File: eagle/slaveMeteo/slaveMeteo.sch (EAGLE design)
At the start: 33 parts, among them J1 RJ12RIGHTANGLE-I2C, Q1 CMA-4544PF-W, U2 MAX4466EXK+T, X1 1503_09

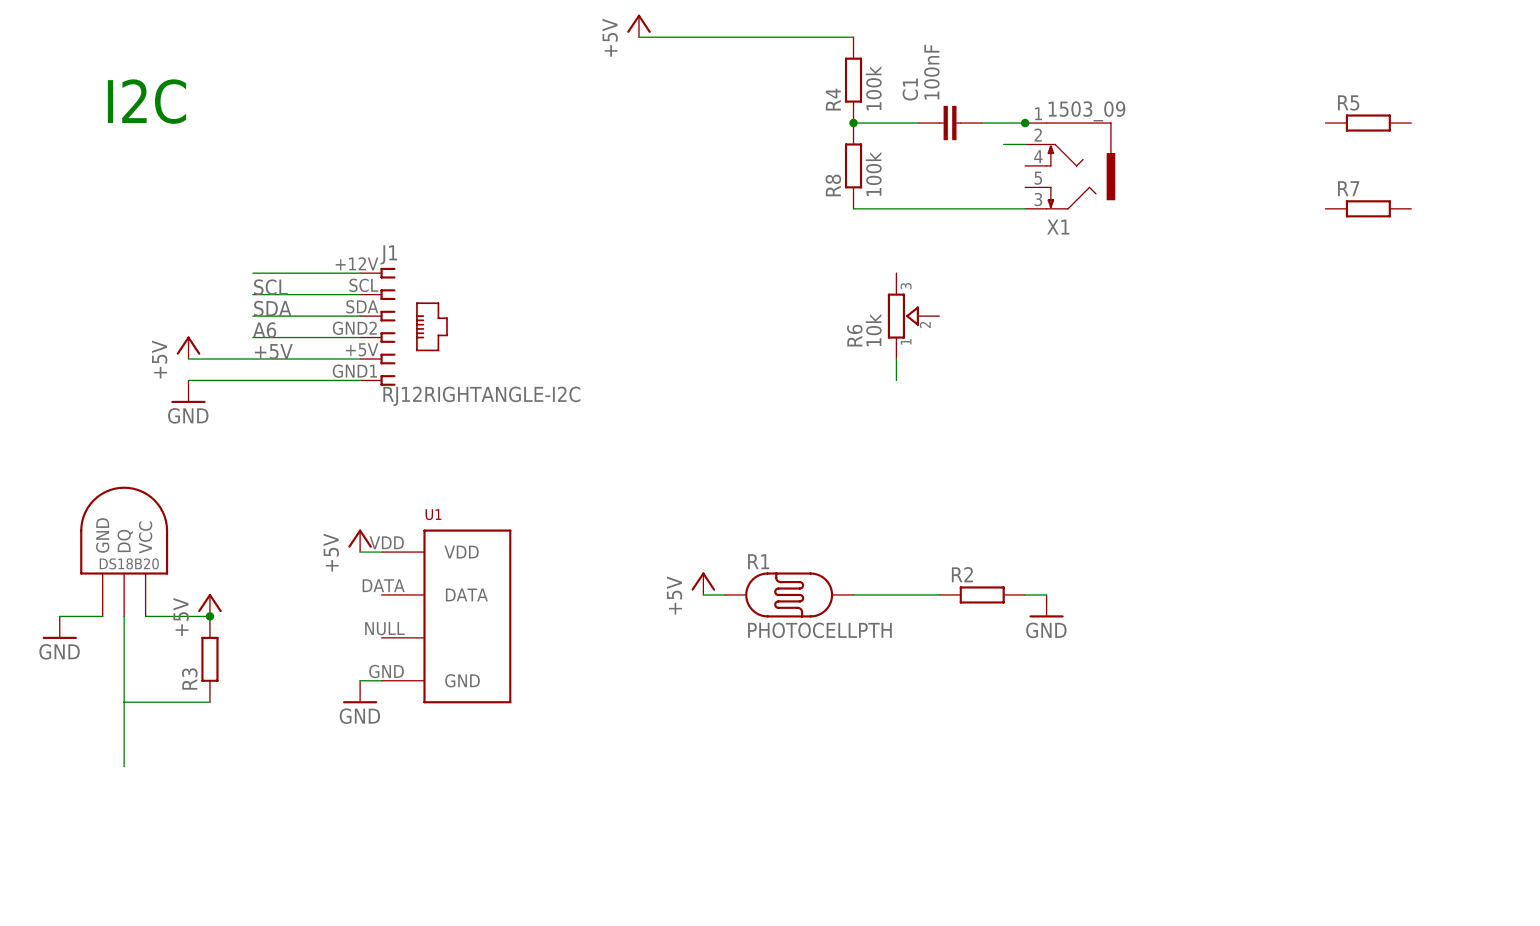
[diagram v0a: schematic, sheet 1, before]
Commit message: updated eagle libraries and readme, started designing meteo station
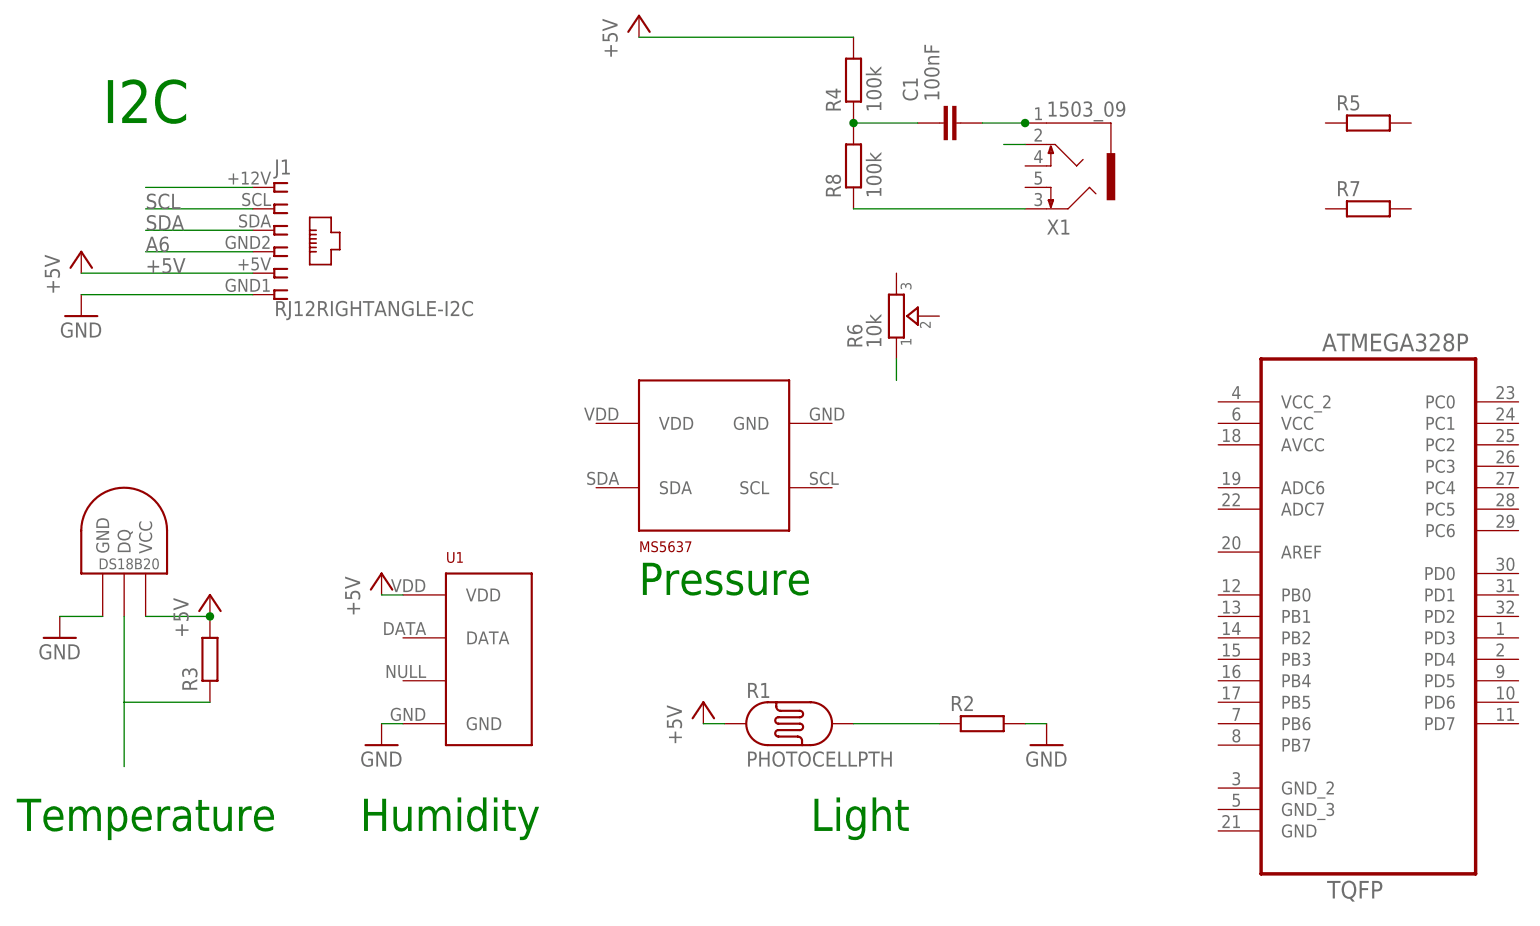
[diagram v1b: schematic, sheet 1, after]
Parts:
- added U$19: MS5637, MS5637:MS5637
- added U3: ATMEGA328P-AU, Ava:ATMEGA328P-AU
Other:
- note added: "Humidity"
- note added: "Light"
- note added: "Pressure"
- note added: "Temperature"
- moved on the sheet: J1, R1, R2, U1
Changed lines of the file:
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@@
 <?xml version="1.0" encoding="utf-8"?>
 <!DOCTYPE eagle SYSTEM "eagle.dtd">
-<eagle version="8.2.2">
+<eagle version="9.0.0">
 <drawing>
 <settings>
 <setting alwaysvectorfont="no"/>
+<setting keepoldvectorfont="yes"/>
 <setting verticaltext="up"/>
 </settings>
@@
 <part name="U$16" library="microbuilder" deviceset="GND" device=""/>
 <part name="P+7" library="microbuilder" deviceset="VCC" device=""/>
+<part name="U3" library="Ava" deviceset="ATMEGA328P-AU" device=""/>
+<part name="U$19" library="MS5637" deviceset="MS5637" device=""/>
 </parts>
 <sheets>
@@
 <plain>
 <text x="48.26" y="73.66" size="5.08" layer="91">I2C</text>
+<text x="38.1" y="-10.16" size="3.81" layer="91">Temperature</text>
+<text x="78.74" y="-10.16" size="3.81" layer="91">Humidity</text>
+<text x="132.08" y="-10.16" size="3.81" layer="91">Light</text>
+<text x="111.76" y="17.78" size="3.81" layer="91">Pressure</text>
 </plain>
 <instances>
-<instance part="GND8" gate="1" x="58.42" y="40.64"/>
-<instance part="J1" gate="G$1" x="81.28" y="50.8"/>
+<instance part="GND8" gate="1" x="45.72" y="50.8"/>
+<instance part="J1" gate="G$1" x="68.58" y="60.96"/>
 <instance part="U$1" gate="G$1" x="50.8" y="20.32"/>
-<instance part="U1" gate="G$1" x="91.44" y="15.24"/>
-<instance part="R1" gate="G$1" x="129.54" y="17.78"/>
-<instance part="R2" gate="G$1" x="152.4" y="17.78"/>
+<instance part="U1" gate="G$1" x="93.98" y="10.16"/>
+<instance part="R1" gate="G$1" x="129.54" y="2.54"/>
+<instance part="R2" gate="G$1" x="152.4" y="2.54"/>
 <instance part="R3" gate="G$1" x="60.96" y="10.16" rot="R90"/>
 <instance part="GND1" gate="1" x="43.18" y="12.7"/>
-<instance part="P+1" gate="1" x="58.42" y="48.26"/>
+<instance part="P+1" gate="1" x="45.72" y="58.42"/>
 <instance part="P+2" gate="1" x="60.96" y="17.78"/>
-<instance part="GND2" gate="1" x="78.74" y="5.08"/>
-<instance part="P+3" gate="1" x="78.74" y="25.4"/>
-<instance part="P+4" gate="1" x="119.38" y="20.32"/>
-<instance part="GND3" gate="1" x="160.02" y="15.24"/>
+<instance part="GND2" gate="1" x="81.28" y="0"/>
+<instance part="P+3" gate="1" x="81.28" y="20.32"/>
+<instance part="P+4" gate="1" x="119.38" y="5.08"/>
+<instance part="GND3" gate="1" x="160.02" y="0"/>
 <instance part="R6" gate="R" x="142.24" y="50.8" rot="R90"/>
 <instance part="X1" gate="G$1" x="162.56" y="68.58" rot="MR180"/>
@@
 <instance part="R8" gate="G$1" x="137.16" y="68.58" rot="R90"/>
 <instance part="P+5" gate="1" x="111.76" y="86.36"/>
+<instance part="U3" gate="A" x="198.12" y="17.78"/>
+<instance part="U$19" gate="G$1" x="121.92" y="35.56"/>
 </instances>
 <busses>
@@
 <segment>
 <pinref part="GND8" gate="1" pin="GND"/>
-<wire x1="78.74" y1="43.18" x2="58.42" y2="43.18" width="0.1524" layer="91"/>
+<wire x1="66.04" y1="53.34" x2="45.72" y2="53.34" width="0.1524" layer="91"/>
 <pinref part="J1" gate="G$1" pin="6"/>
 </segment>
@@
 <pinref part="U1" gate="G$1" pin="GND"/>
 <pinref part="GND2" gate="1" pin="GND"/>
-<wire x1="78.74" y1="7.62" x2="81.28" y2="7.62" width="0.1524" layer="91"/>
+<wire x1="81.28" y1="2.54" x2="83.82" y2="2.54" width="0.1524" layer="91"/>
 </segment>
 <segment>
 <pinref part="R2" gate="G$1" pin="2"/>
 <pinref part="GND3" gate="1" pin="GND"/>
-<wire x1="160.02" y1="17.78" x2="157.48" y2="17.78" width="0.1524" layer="91"/>
+<wire x1="160.02" y1="2.54" x2="157.48" y2="2.54" width="0.1524" layer="91"/>
 </segment>
 <segment>
@@
 <net name="SDA" class="0">
 <segment>
-<wire x1="78.74" y1="50.8" x2="66.04" y2="50.8" width="0.1524" layer="91"/>
-<label x="66.04" y="50.8" size="1.778" layer="95"/>
+<wire x1="66.04" y1="60.96" x2="53.34" y2="60.96" width="0.1524" layer="91"/>
+<label x="53.34" y="60.96" size="1.778" layer="95"/>
 <pinref part="J1" gate="G$1" pin="3"/>
 </segment>
@@
 <net name="SCL" class="0">
 <segment>
-<wire x1="78.74" y1="53.34" x2="66.04" y2="53.34" width="0.1524" layer="91"/>
-<label x="66.04" y="53.34" size="1.778" layer="95"/>
+<wire x1="66.04" y1="63.5" x2="53.34" y2="63.5" width="0.1524" layer="91"/>
+<label x="53.34" y="63.5" size="1.778" layer="95"/>
 <pinref part="J1" gate="G$1" pin="2"/>
 </segment>
@@
 <net name="A6" class="0">
 <segment>
-<wire x1="66.04" y1="48.26" x2="78.74" y2="48.26" width="0.1524" layer="91"/>
+<wire x1="53.34" y1="58.42" x2="66.04" y2="58.42" width="0.1524" layer="91"/>
 <pinref part="J1" gate="G$1" pin="4"/>
-<label x="66.04" y="48.26" size="1.778" layer="95"/>
+<label x="53.34" y="58.42" size="1.778" layer="95"/>
 </segment>
 </net>
@@
 <pinref part="R1" gate="G$1" pin="P$2"/>
 <pinref part="R2" gate="G$1" pin="1"/>
-<wire x1="137.16" y1="17.78" x2="147.32" y2="17.78" width="0.1524" layer="91"/>
+<wire x1="137.16" y1="2.54" x2="147.32" y2="2.54" width="0.1524" layer="91"/>
 </segment>
 </net>
@@
 <segment>
 <pinref part="J1" gate="G$1" pin="5"/>
-<wire x1="78.74" y1="45.72" x2="58.42" y2="45.72" width="0.1524" layer="91"/>
-<label x="66.04" y="45.72" size="1.778" layer="95"/>
+<wire x1="66.04" y1="55.88" x2="45.72" y2="55.88" width="0.1524" layer="91"/>
+<label x="53.34" y="55.88" size="1.778" layer="95"/>
 <pinref part="P+1" gate="1" pin="+5V"/>
 </segment>
@@
 <pinref part="U1" gate="G$1" pin="VDD"/>
 <pinref part="P+3" gate="1" pin="+5V"/>
-<wire x1="78.74" y1="22.86" x2="81.28" y2="22.86" width="0.1524" layer="91"/>
+<wire x1="81.28" y1="17.78" x2="83.82" y2="17.78" width="0.1524" layer="91"/>
 </segment>
 <segment>
 <pinref part="R1" gate="G$1" pin="P$1"/>
 <pinref part="P+4" gate="1" pin="+5V"/>
-<wire x1="119.38" y1="17.78" x2="121.92" y2="17.78" width="0.1524" layer="91"/>
+<wire x1="119.38" y1="2.54" x2="121.92" y2="2.54" width="0.1524" layer="91"/>
 </segment>
 <segment>
@@
 <segment>
 <pinref part="J1" gate="G$1" pin="1"/>
-<wire x1="78.74" y1="55.88" x2="66.04" y2="55.88" width="0.1524" layer="91"/>
+<wire x1="66.04" y1="66.04" x2="53.34" y2="66.04" width="0.1524" layer="91"/>
 </segment>
 </net>
@@
 <compatibility>
 <note version="8.2" severity="warning">
-Since Version 8.2, Eagle supports online libraries. The ids
+Since Version 8.2, EAGLE supports online libraries. The ids
 of those online libraries will not be understood (or retained)
 with this version.

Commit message: connected components on Slave meteo. Kept backup in case we still need a sound detector
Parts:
- removed C5: 10uF, microbuilder:CAP_CERAMIC0805
- removed FB1, FB2: FERRITE, microbuilder:FERRITE0805
- removed FID1, FID2: FIDUCIAL"", microbuilder:FIDUCIAL""
- removed JP1: (no value), microbuilder:HEADER-1X376MIL
- removed Q1: CMA-4544PF-W, microbuilder:ELECTRET
- removed R10, R11: 1K, microbuilder:RESISTOR0805
- removed R12, R13: 1M, microbuilder:RESISTOR0805
- removed R14: 22K, microbuilder:RESISTOR0805
- removed U$14, U$15: MOUNTINGHOLE2.5, microbuilder:MOUNTINGHOLE2.5
- removed U2: MAX4466EXK+T, microbuilder:MAX4466""
- removed VR1: TC33X-2-104E (100K), microbuilder:TRIMPOTTC33X-2
- added S1: Reset, Testing:SWITCH-MOMENTARY-2SMD-ALT01
- C2: value 0.1µF -> 100nF; device microbuilder:CAP_CERAMIC0805 -> rcl:C-EUC0805K; ELECROW (none) -> C49678; LCSC (none) -> C49678; MPN (none) -> 80-C1206C104K5R
- C3: value 0.01uF -> 100nF; device microbuilder:CAP_CERAMIC0805 -> rcl:C-EUC0805K; ELECROW (none) -> C49678; LCSC (none) -> C49678; MPN (none) -> 80-C1206C104K5R
- C4: value 100pF -> 100nF; device microbuilder:CAP_CERAMIC0805 -> rcl:C-EUC0805K; ELECROW (none) -> C49678; LCSC (none) -> C49678; MPN (none) -> 80-C1206C104K5R
- R9: value 1K -> 10k; device microbuilder:RESISTOR0805 -> rcl:R-EU_R0805; ELECROW (none) -> C17513; LCSC (none) -> C17513
- U3: value ATMEGA328P-AU -> ATMEGA328; device Ava:ATMEGA328P-AU -> SparkFun:ATMEGA168
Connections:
- removed net AGND: C2.P$2, C5.P$2, FB1.P$2, Q1.1, R12.1, U2.GND
- removed net AVCC: FB2.P$1, R10.2, R13.2, U2.VCC
- removed net N$1: R1.P$2, R2.1
- removed net N$10: C5.P$1, R11.1
- removed net N$11: R14.2, VR1.E
- removed net N$2: C3.P$1, Q1.2, R9.1
- removed net N$3: R3.1, U$1.DQ
- removed net N$6: C2.P$1, R10.1, R9.2
- removed net N$7: C3.P$2, R12.2, R13.1, U2.IN+
- removed net N$8: C4.P$1, JP1.3, U2.OUT, VR1.A, VR1.S
- removed net N$9: C4.P$2, R11.2, R14.1, U2.IN-
- new net 3.3V: J1.5
- new net A0: R3.1, U$1.DQ, U3.PC0(ADC0)
- new net A1: R1.P$2, R2.1, U3.PC1(ADC1)
- new net A2: U1.DATA, U3.PC2(ADC2)
- new net A3: U3.PC3(ADC3)
- new net A7: U3.ADC7
- new net AREF: C3.1, U3.AREF
- new net D10: U3.PB2(SS/OC1B)
- new net D2: U3.PD2(INT0)
- new net D3: U3.PD3(INT1)
- new net D4: U3.PD4(XCK/T0)
- new net D5: U3.PD5(T1)
- new net D6: U3.PD6(AIN0)
- new net D7: U3.PD7(AIN1)
- new net D8: U3.PB0(ICP)
- new net D9: U3.PB1(OC1A)
- new net DTR: C2.1
- new net MISO: U3.PB4(MISO)
- new net MOSI: U3.PB3(MOSI/OC2)
- new net RESET: C2.2, R9.1, S1.2, U3.PC6(/RESET)
- new net RX: U3.PD0(RXD)
- new net SCK: U3.PB5(SCK)
- new net TX: U3.PD1(TXD)
- net +5V: no longer J1.5
- net A6: now also U3.ADC6
- net GND: now also C3.2, C4.2, S1.1, U$19.GND, U3.AGND, U3.GND@1, U3.GND@2; no longer FB1.P$1, JP1.2
- net SCL: now also U$19.SCL, U3.PC5(ADC5/SCL)
- net SDA: now also U$19.SDA, U3.PC4(ADC4/SDA)
- net VCC: now also C4.1, R9.2, U$19.VDD, U3.AVCC, U3.VCC@1, U3.VCC@2; no longer FB2.P$2, JP1.1
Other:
- note added: "ATMega328"
- note removed: "+1"
- note removed: "= ~25-125x gain"
- note removed: "Gain ="
- note removed: "Low pass F3db = 1/R5*C4*2pi"
- note removed: "R5"
- note removed: "VR1+R7"
